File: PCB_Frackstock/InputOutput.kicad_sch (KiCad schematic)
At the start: 31 parts, among them J1 87224-3, Q2 BSS138, U11 CC1101RGPR, U7 BMI160, Y2 JGHC S3226000151040

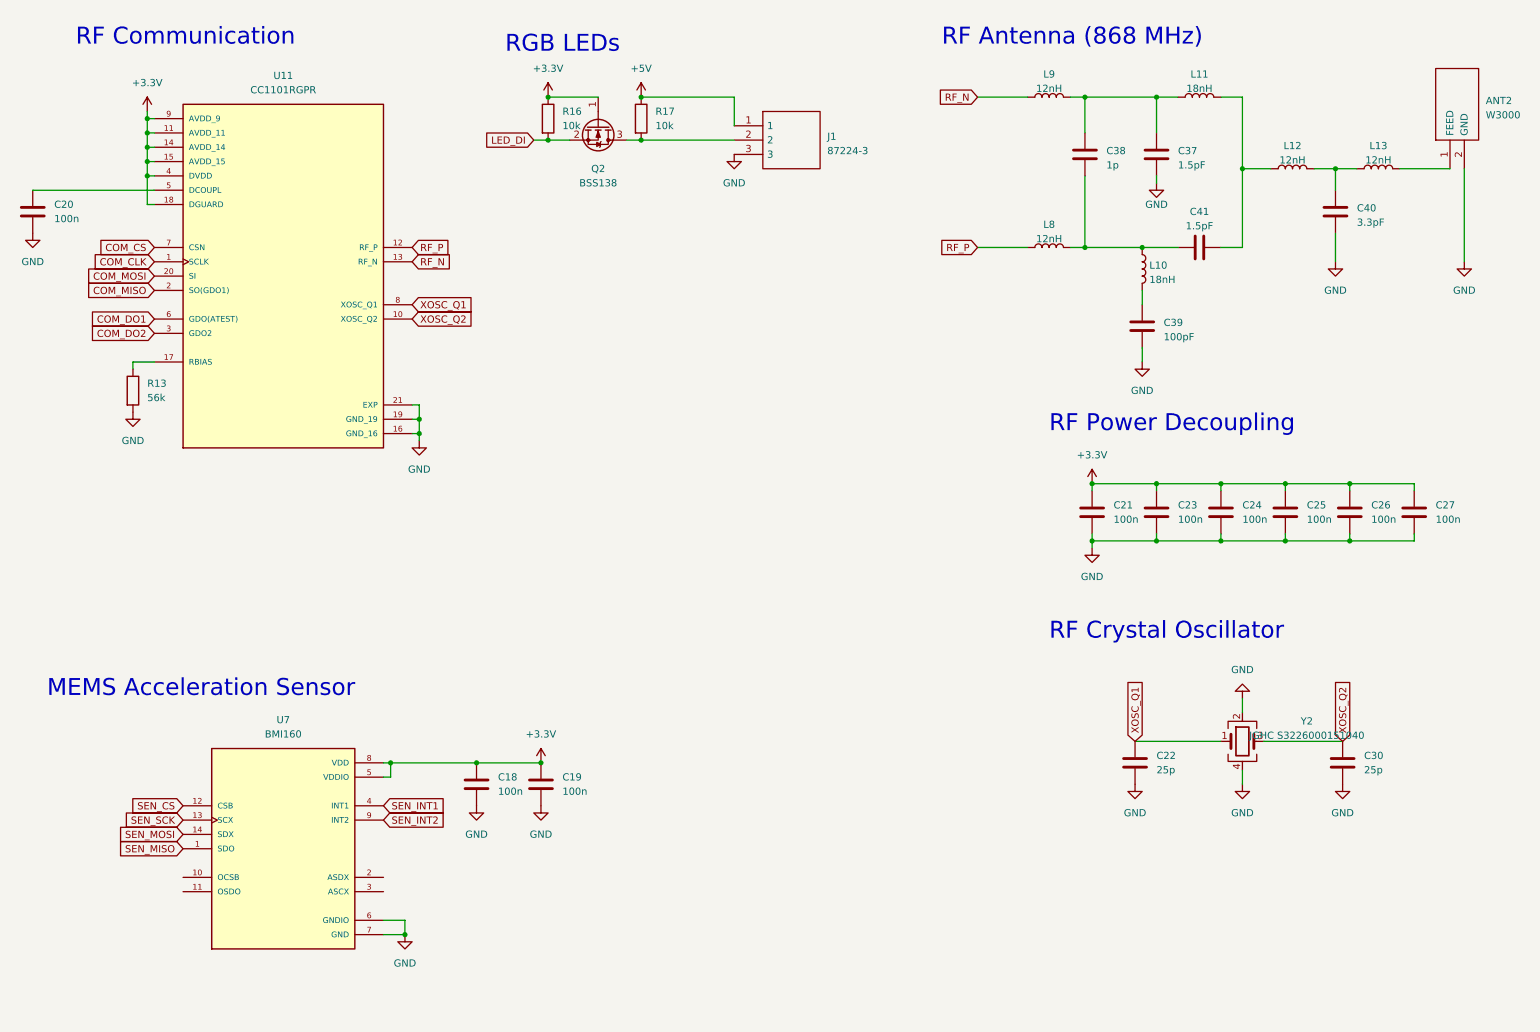
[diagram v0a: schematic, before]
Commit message: Battery Management and change parts to 0603
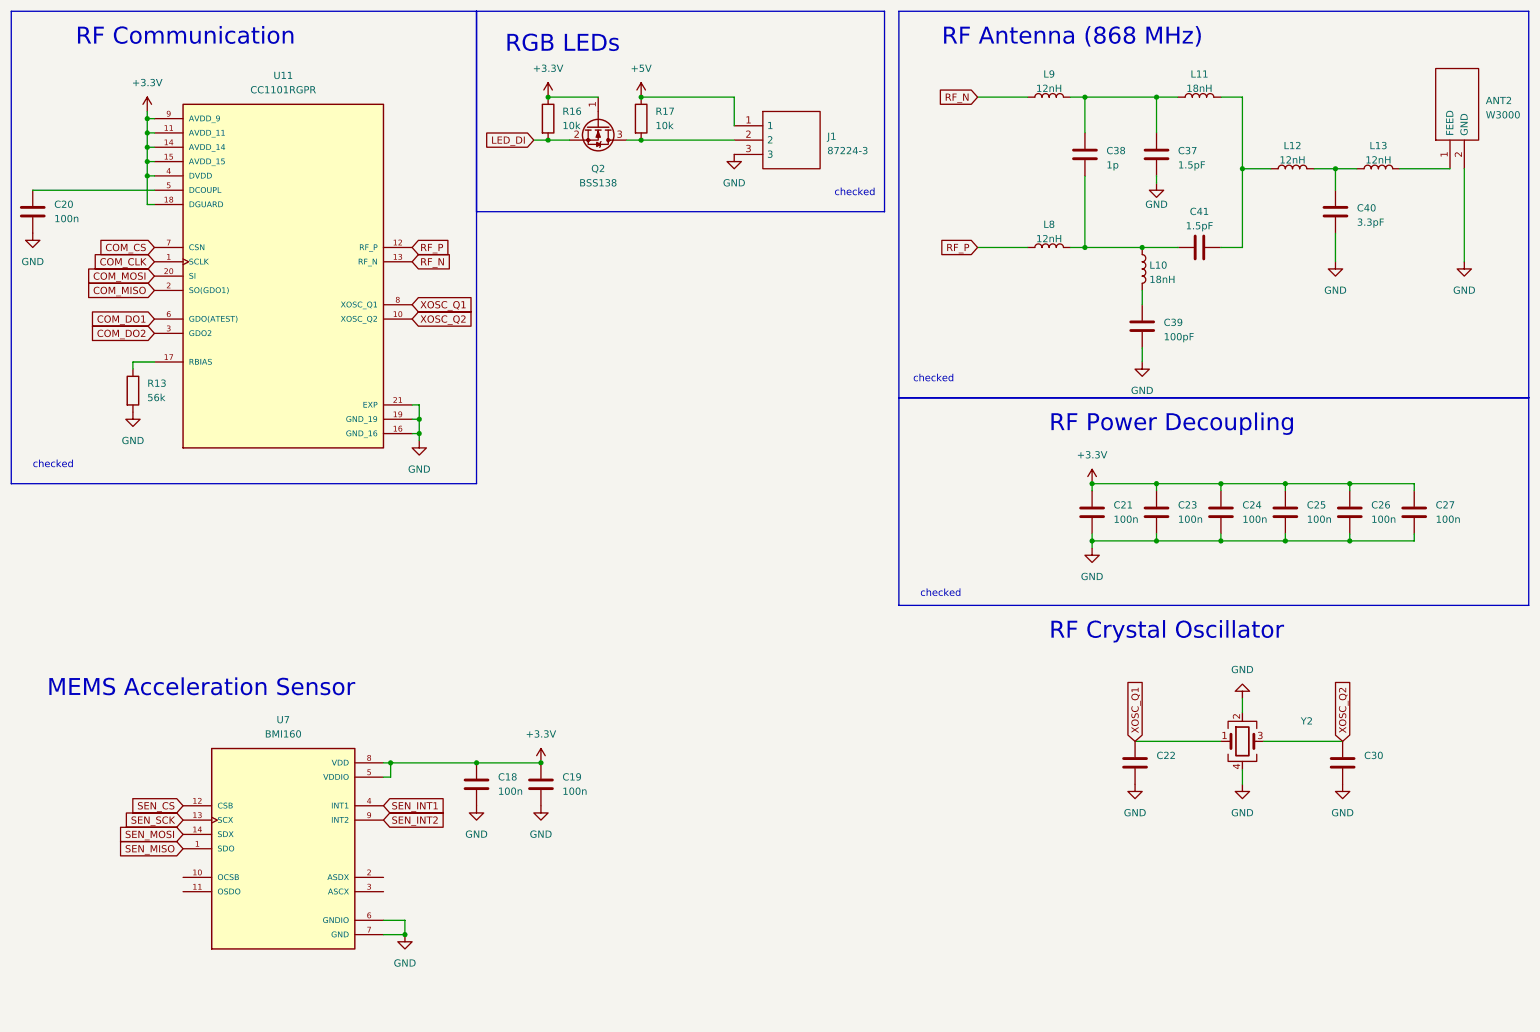
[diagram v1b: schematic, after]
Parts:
- C20: footprint Capacitor_SMD:C_0201_0603Metric -> Capacitor_SMD:C_0603_1608Metric_Pad1.08x0.95mm_HandSolder; LCSC C66938 -> (none); Note https://www.lcsc.com/product-detail/Multilayer-Ceramic-Capa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 -> (none); Vendor C30926 -> (none); vendor C30926 -> (none)
- C22, C30: value 25p -> ~
- Q2: LCSC C2938375 -> (none); Note https://www.lcsc.com/product-detail/MOSFETs_GOODWORK-BSS138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 -> (none); Vendor C3040446 -> (none); vendor C3040446 -> (none)
- R13: footprint Resistor_SMD:R_0201_0603Metric -> Resistor_SMD:R_0603_1608Metric_Pad0.98x0.95mm_HandSolder; LCSC C851761 -> (none); Note https://www.lcsc.com/product-detail/Chip-Resistor-Surface-M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 -> (none); Vendor C23206 -> (none); vendor C23206 -> (none)
- R16, R17: footprint Resistor_SMD:R_0201_0603Metric -> Resistor_SMD:R_0603_1608Metric_Pad0.98x0.95mm_HandSolder; LCSC C106225 -> (none); Note https://www.lcsc.com/product-detail/Chip-Resistor-Surface-M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 -> (none); Vendor C25804 -> (none); vendor C25804 -> (none)
- Y2: value JGHC S3226000151040 -> ~; footprint Crystal:Crystal_SMD_3225-4Pin_3.2x2.5mm -> (none); Note https://www.lcsc.com/product-detail/Crystals_span-style-bac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 -> https://www.mouser.ch/ProductDetail/CTS-Electronic-Componen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
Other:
- note added: "checked"

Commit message: Schema fertig
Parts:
- removed Q2: BSS138, Package_TO_SOT_SMD:SOT-23, symbol Transistor_FET:BSS138
- removed R17: 10k, Resistor_SMD:R_0603_1608Metric_Pad0.98x0.95mm_HandSolder, symbol Device:R
- added C33: 1000u, Capacitor_SMD:CP_Elec_8x10.5, symbol Device:C
- ANT2: footprint KiCad:W3000 -> RF_Antenna:W3000
- C18, C19: footprint Capacitor_SMD:C_0201_0603Metric -> Capacitor_SMD:C_0603_1608Metric_Pad1.08x0.95mm_HandSolder
- C22, C30: value ~ -> 20p
- R16: value 10k -> 470
- U7: value BMI160 -> BMI323; LCSC C94021 -> (none); MANUFACTURER Bosch -> (none); MAXIMUM_PACKAGE_HEIGHT 0.88 mm -> (none); Note https://www.lcsc.com/product-detail/Attitude-Sensor-Gyrosco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 -> (none); PARTREV 1.0 -> (none); STANDARD IPC 7351B -> (none); Vendor C94021 -> (none); vendor C94021 -> (none)
- Y2: value ~ -> 26MHz; footprint (none) -> Crystal:Crystal_SMD_Abracon_ABM3B-4Pin_5.0x3.2mm
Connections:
- net +3.3V: no longer R16.1
- net GND: now also C33.1
- net LED_DI: now also R16.1; no longer R16.2
- net at J1.2: now also R16.2
- net +5V renamed BAT_O
- net BAT_O: now also C33.2

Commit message: Schema_fertig
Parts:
- removed J1: 87224-3, KiCad:872243, symbol 87224-3:87224-3
- added J1: Conn_01x03_Pin, Connector_PinHeader_2.54mm:PinHeader_1x03_P2.54mm_Vertical, symbol Connector:Conn_01x03_Pin
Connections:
- net BAT_O: now also J1.3 (Pin_3)
- net GND: now also J1.1 (Pin_1)
- net at R16.2: now also J1.2 (Pin_2)
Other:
- moved on the sheet: C33, R16

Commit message: Layout Fertig
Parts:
- removed J1: Conn_01x03_Pin, Connector_PinHeader_2.54mm:PinHeader_1x03_P2.54mm_Vertical, symbol Connector:Conn_01x03_Pin
- added J1: Conn_01x06_Pin, symbol Connector:Conn_01x06_Pin
- C33: value 1000u -> 330u; footprint Capacitor_SMD:CP_Elec_8x10.5 -> Capacitor_SMD:C_0805_2012Metric_Pad1.18x1.45mm_HandSolder
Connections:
- net +3.3V: now also J1.4 (Pin_4)
- net BAT_O: now also J1.3 (Pin_3)
- net GND: now also J1.1 (Pin_1)
- net at R16.2: now also J1.2 (Pin_2)
- new net SCL: J1.6 (Pin_6)
- new net SDA: J1.5 (Pin_5)
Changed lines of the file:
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@@
   (junction (at 228.6 97.79) (diameter 0) (color 0 0 0 0)
   )
+  (junction (at 134.62 34.29) (diameter 0) (color 0 0 0 0)
+  )
   (junction (at 83.82 177.8) (diameter 0) (color 0 0 0 0)
   )
-  (junction (at 134.62 39.37) (diameter 0) (color 0 0 0 0)
-  )
   (junction (at 240.03 107.95) (diameter 0) (color 0 0 0 0)
   )
@@
     (stroke (width 0) (type default))
   )
+  (wire (pts (xy 143.51 46.99) (xy 148.59 46.99))
+    (stroke (width 0) (type default))
+  )
   (wire (pts (xy 38.1 40.64) (xy 38.1 38.1))
     (stroke (width 0) (type default))
@@
     (stroke (width 0) (type default))
   )
+  (wire (pts (xy 134.62 34.29) (xy 148.59 34.29))
+    (stroke (width 0) (type default))
+  )
+  (wire (pts (xy 134.62 34.29) (xy 134.62 50.8))
+    (stroke (width 0) (type default))
+  )
   (wire (pts (xy 185.42 55.88) (xy 194.31 55.88))
     (stroke (width 0) (type default))
   )
-  (wire (pts (xy 134.62 31.75) (xy 134.62 39.37))
-    (stroke (width 0) (type default))
-  )
   (wire (pts (xy 232.41 41.91) (xy 237.49 41.91))
     (stroke (width 0) (type default))
@@
     (stroke (width 0) (type default))
   )
+  (wire (pts (xy 138.43 41.91) (xy 148.59 41.91))
+    (stroke (width 0) (type default))
+  )
   (wire (pts (xy 134.62 22.86) (xy 134.62 24.13))
     (stroke (width 0) (type default))
@@
     (stroke (width 0) (type default))
   )
-  (wire (pts (xy 130.81 36.83) (xy 143.51 36.83))
+  (wire (pts (xy 130.81 36.83) (xy 148.59 36.83))
     (stroke (width 0) (type default))
   )
@@
     (stroke (width 0) (type default))
   )
-  (wire (pts (xy 134.62 39.37) (xy 134.62 43.18))
+  (wire (pts (xy 134.62 31.75) (xy 134.62 34.29))
     (stroke (width 0) (type default))
   )
@@
     (stroke (width 0) (type default))
   )
+  (wire (pts (xy 143.51 44.45) (xy 148.59 44.45))
+    (stroke (width 0) (type default))
+  )
   (wire (pts (xy 251.46 97.79) (xy 251.46 99.06))
     (stroke (width 0) (type default))
@@
     (stroke (width 0) (type default))
   )
-  (wire (pts (xy 143.51 22.86) (xy 143.51 34.29))
+  (wire (pts (xy 143.51 22.86) (xy 143.51 39.37))
+    (stroke (width 0) (type default))
+  )
+  (wire (pts (xy 143.51 39.37) (xy 148.59 39.37))
     (stroke (width 0) (type default))
   )
@@
     (stroke (width 0) (type default))
   )
-  (wire (pts (xy 134.62 39.37) (xy 143.51 39.37))
-    (stroke (width 0) (type default))
-  )
   (wire (pts (xy 232.41 55.88) (xy 228.6 55.88))
     (stroke (width 0) (type default))
@@
     (stroke (width 0) (type default))
   )
-  (rectangle (start 97.79 13.97) (end 170.18 49.53)
+  (rectangle (start 97.79 13.97) (end 170.18 68.58)
     (stroke (width 0) (type default))
     (fill (type none))
@@
     )
   )
+  (global_label "SDA" (shape input) (at 143.51 44.45 180) (fields_autoplaced)
+    (effects (font (size 1.27 1.27)) (justify right))
+    (property "Intersheetrefs" "${INTERSHEET_REFS}" (at 137.0361 44.45 0)
+      (effects (font (size 1.27 1.27)) (justify right) hide)
+    )
+  )
   (global_label "RF_P" (shape input) (at 185.42 55.88 180) (fields_autoplaced)
     (effects (font (size 1.27 1.27)) (justify right))
@@
     )
   )
+  (global_label "SCL" (shape input) (at 143.51 46.99 180) (fields_autoplaced)
+    (effects (font (size 1.27 1.27)) (justify right))
+    (property "Intersheetrefs" "${INTERSHEET_REFS}" (at 137.0966 46.99 0)
+      (effects (font (size 1.27 1.27)) (justify right) hide)
+    )
+  )
   (global_label "XOSC_Q2" (shape input) (at 85.09 68.58 0) (fields_autoplaced)
     (effects (font (size 1.27 1.27)) (justify left))
@@
         (path "/d92252e1-c687-49e6-87c8-e9430a2c933e/c15a2309-71af-495b-84ee-43442cf95a1c"
           (reference "#PWR019") (unit 1)
+        )
+      )
+    )
+  )
+  (symbol (lib_id "power:+3.3V") (at 138.43 41.91 0) (unit 1)
+    (in_bom yes) (on_board yes) (dnp no)
+    (property "Reference" "#PWR03" (at 138.43 45.72 0)
+      (effects (font (size 1.27 1.27)) hide)
+    )
+    (property "Value" "+3.3V" (at 139.7 38.1 0)
+      (effects (font (size 1.27 1.27)))
+    )
+    (property "Footprint" "" (at 138.43 41.91 0)
+      (effects (font (size 1.27 1.27)) hide)
+    )
+    (property "Datasheet" "" (at 138.43 41.91 0)
+      (effects (font (size 1.27 1.27)) hide)
+    )
+    (pin "1")
+    (instances
+      (project "Frackstock"
+        (path "/d92252e1-c687-49e6-87c8-e9430a2c933e/c15a2309-71af-495b-84ee-43442cf95a1c"
+          (reference "#PWR03") (unit 1)
         )
       )
@@
     )
   )
-  (symbol (lib_id "power:GND") (at 134.62 43.18 0) (unit 1)
-    (in_bom yes) (on_board yes) (dnp no) (fields_autoplaced)
-    (property "Reference" "#PWR013" (at 134.62 49.53 0)
-      (effects (font (size 1.27 1.27)) hide)
-    )
-    (property "Value" "GND" (at 134.62 48.26 0)
-      (effects (font (size 1.27 1.27)))
-    )
-    (property "Footprint" "" (at 134.62 43.18 0)
-      (effects (font (size 1.27 1.27)) hide)
-    )
-    (property "Datasheet" "" (at 134.62 43.18 0)
+  (symbol (lib_id "power:GND") (at 134.62 50.8 0) (unit 1)
+    (in_bom yes) (on_board yes) (dnp no) (fields_autoplaced)
+    (property "Reference" "#PWR013" (at 134.62 57.15 0)
+      (effects (font (size 1.27 1.27)) hide)
+    )
+    (property "Value" "GND" (at 134.62 55.88 0)
+      (effects (font (size 1.27 1.27)))
+    )
+    (property "Footprint" "" (at 134.62 50.8 0)
+      (effects (font (size 1.27 1.27)) hide)
+    )
+    (property "Datasheet" "" (at 134.62 50.8 0)
       (effects (font (size 1.27 1.27)) hide)
     )
@@
       (effects (font (size 1.27 1.27)) (justify right))
     )
-    (property "Value" "1000u" (at 138.43 29.845 0)
+    (property "Value" "330u" (at 138.43 29.845 0)
       (effects (font (size 1.27 1.27)) (justify right))
     )
-    (property "Footprint" "Capacitor_SMD:CP_Elec_8x10.5" (at 133.6548 24.13 0)
+    (property "Footprint" "Capacitor_SMD:C_0805_2012Metric_Pad1.18x1.45mm_HandSolder" (at 133.6548 24.13 0)
       (effects (font (size 1.27 1.27)) hide)
     )
@@
         (path "/d92252e1-c687-49e6-87c8-e9430a2c933e/c15a2309-71af-495b-84ee-43442cf95a1c"
           (reference "C37") (unit 1)
+        )
+      )
+    )
+  )
+  (symbol (lib_id "Connector:Conn_01x06_Pin") (at 153.67 39.37 0) (mirror y) (unit 1)
+    (in_bom yes) (on_board yes) (dnp no) (fields_autoplaced)
+    (property "Reference" "J1" (at 154.94 40.005 0)
+      (effects (font (size 1.27 1.27)) (justify right))
+    )
+    (property "Value" "Conn_01x06_Pin" (at 154.94 42.545 0)
+      (effects (font (size 1.27 1.27)) (justify right))
+    )
+    (property "Footprint" "" (at 153.67 39.37 0)
+      (effects (font (size 1.27 1.27)) hide)
+    )
+    (property "Datasheet" "~" (at 153.67 39.37 0)
+      (effects (font (size 1.27 1.27)) hide)
+    )
+    (pin "1")
+    (pin "2")
+    (pin "3")
+    (pin "4")
+    (pin "5")
+    (pin "6")
+    (instances
+      (project "Frackstock"
+        (path "/d92252e1-c687-49e6-87c8-e9430a2c933e/c15a2309-71af-495b-84ee-43442cf95a1c"
+          (reference "J1") (unit 1)
         )
       )
@@
         )
       )
-    )
-  )
-  (symbol (lib_id "Connector:Conn_01x03_Pin") (at 148.59 36.83 180) (unit 1)
-    (in_bom yes) (on_board yes) (dnp no) (fields_autoplaced)
-    (property "Reference" "J1" (at 149.86 35.56 0)
-      (effects (font (size 1.27 1.27)) (justify right))
-    )
-    (property "Value" "Conn_01x03_Pin" (at 149.86 38.1 0)
-      (effects (font (size 1.27 1.27)) (justify right))
-    )
-    (property "Footprint" "Connector_PinHeader_2.54mm:PinHeader_1x03_P2.54mm_Vertical" (at 148.59 36.83 0)
-      (effects (font (size 1.27 1.27)) hide)
-    )
-    (property "Datasheet" "~" (at 148.59 36.83 0)
-      (effects (font (size 1.27 1.27)) hide)
-    )
-    (pin "1")
-    (pin "2")
-    (pin "3")
-    (instances
-      (project "Frackstock"
-        (path "/d92252e1-c687-49e6-87c8-e9430a2c933e/c15a2309-71af-495b-84ee-43442cf95a1c"
-          (reference "J1") (unit 1)
-        )
-      )

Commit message: Layout Update
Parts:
- J1: footprint (none) -> Frack:PinHeader_2x03_P2.54mm_Vertical_SMD_kleiner
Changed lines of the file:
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@@
       (effects (font (size 1.27 1.27)) (justify right))
     )
-    (property "Footprint" "" (at 153.67 39.37 0)
+    (property "Footprint" "Frack:PinHeader_2x03_P2.54mm_Vertical_SMD_kleiner" (at 153.67 39.37 0)
       (effects (font (size 1.27 1.27)) hide)
     )

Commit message: USB Differenziell
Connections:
- net +3.3V: now also J1.3 (Pin_3); no longer J1.4 (Pin_4)
- net BAT_O: now also J1.4 (Pin_4); no longer J1.3 (Pin_3)
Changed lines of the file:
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@@
+    (stroke (width 0) (type default))
+  )
+  (wire (pts (xy 146.05 31.75) (xy 146.05 39.37))
     (stroke (width 0) (type default))
   )
@@
     (stroke (width 0) (type default))
   )
+  (wire (pts (xy 143.51 22.86) (xy 143.51 41.91))
+    (stroke (width 0) (type default))
+  )
   (wire (pts (xy 271.78 41.91) (xy 271.78 58.42))
     (stroke (width 0) (type default))
@@
     (stroke (width 0) (type default))
   )
-  (wire (pts (xy 138.43 41.91) (xy 148.59 41.91))
-    (stroke (width 0) (type default))
-  )
   (wire (pts (xy 134.62 22.86) (xy 134.62 24.13))
     (stroke (width 0) (type default))
@@
     (stroke (width 0) (type default))
   )
+  (wire (pts (xy 143.51 41.91) (xy 148.59 41.91))
+    (stroke (width 0) (type default))
+  )
   (wire (pts (xy 85.09 83.82) (xy 86.36 83.82))
     (stroke (width 0) (type default))
@@
     (stroke (width 0) (type default))
   )
-  (wire (pts (xy 143.51 22.86) (xy 143.51 39.37))
-    (stroke (width 0) (type default))
-  )
-  (wire (pts (xy 143.51 39.37) (xy 148.59 39.37))
-    (stroke (width 0) (type default))
-  )
   (wire (pts (xy 39.37 38.1) (xy 38.1 38.1))
     (stroke (width 0) (type default))
@@
   )
   (wire (pts (xy 232.41 55.88) (xy 228.6 55.88))
+    (stroke (width 0) (type default))
+  )
+  (wire (pts (xy 146.05 39.37) (xy 148.59 39.37))
     (stroke (width 0) (type default))
   )
@@
     )
   )
-  (symbol (lib_id "power:+3.3V") (at 138.43 41.91 0) (unit 1)
+  (symbol (lib_id "power:+3.3V") (at 146.05 31.75 0) (unit 1)
     (in_bom yes) (on_board yes) (dnp no)
-    (property "Reference" "#PWR03" (at 138.43 45.72 0)
-      (effects (font (size 1.27 1.27)) hide)
-    )
-    (property "Value" "+3.3V" (at 139.7 38.1 0)
-      (effects (font (size 1.27 1.27)))
-    )
-    (property "Footprint" "" (at 138.43 41.91 0)
-      (effects (font (size 1.27 1.27)) hide)
-    )
-    (property "Datasheet" "" (at 138.43 41.91 0)
-      (effects (font (size 1.27 1.27)) hide)
-    )
+    (property "Reference" "#PWR03" (at 146.05 35.56 0)
+      (effects (font (size 1.27 1.27)) hide)
+    )
+    (property "Value" "+3.3V" (at 147.32 27.94 0)
+      (effects (font (size 1.27 1.27)))
+    )
+    (property "Footprint" "" (at 146.05 31.75 0)
+      (effects (font (size 1.27 1.27)) hide)
+    )
+    (property "Datasheet" "" (at 146.05 31.75 0)
+      (effects (font (size 1.27 1.27)) hide)
+    )

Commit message: Schema-review-1
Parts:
- removed C18, C19: 100n, Capacitor_SMD:C_0603_1608Metric_Pad1.08x0.95mm_HandSolder, symbol Device:C
- removed C33: 330u, Capacitor_SMD:C_0805_2012Metric_Pad1.18x1.45mm_HandSolder, symbol Device:C
- removed J1: Conn_01x06_Pin, Frack:PinHeader_2x03_P2.54mm_Vertical_SMD_kleiner, symbol Connector:Conn_01x06_Pin
- removed R16: 470, Resistor_SMD:R_0603_1608Metric_Pad0.98x0.95mm_HandSolder, symbol Device:R
- removed U7: BMI323, SnapEDA Library:PQFN50P250X300X88-14N, symbol BMI160:BMI160
- added R12: 10k, Resistor_SMD:R_0603_1608Metric_Pad0.98x0.95mm_HandSolder, symbol Device:R
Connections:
- net +3.3V: now also R12.1
- net COM_CS: now also R12.2
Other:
- note removed: "MEMS Acceleration Sensor"
- note removed: "RF Power Decoupling"
- note removed: "RGB LEDs"
- note removed: "checked"
- company: (none) -> Eberkreis
- title: (none) -> Frackstock ET2024
- moved on the sheet: ANT2, C20, C21, C22, C23, C24, C25, C26, C27, C30, C37, C38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

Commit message: Fracstock PCB final commit
DRC check, PCB review done, ready to order
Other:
- company: Eberkreis -> Eberkreis Engineering
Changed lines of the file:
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@@
     (date "2024-03-24")
     (rev "2")
-    (company "Eberkreis")
+    (company "Eberkreis Engineering")
   )
   (junction (at 78.74 33.02) (diameter 0) (color 0 0 0 0)
